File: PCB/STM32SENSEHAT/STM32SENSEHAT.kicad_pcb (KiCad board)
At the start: 2 copper layers, 100 x 100 mm, 78 parts, among them J1 USB_B_Micro, J10 Conn_01x01_Pin, J11 Conn_01x02_Pin, J2 Conn_01x05_Pin, J5 Conn_01x24_Pin, J8 Conn_01x24_Pin, J9 Conn_01x10_Pin, Q1 FS8205A, SW1 SW_Push, U1 MCP1700x-330xxTT, U11 AO3401A_C306862, U2 DW01A, U3 FT234XD-R, U4 TMP102xxDRL, U5 CAT24C256, U6 LTR-303ALS-01, U7 TP4056, U9 STLINK_UCT, X1 XXDCELNANF-8MHZ

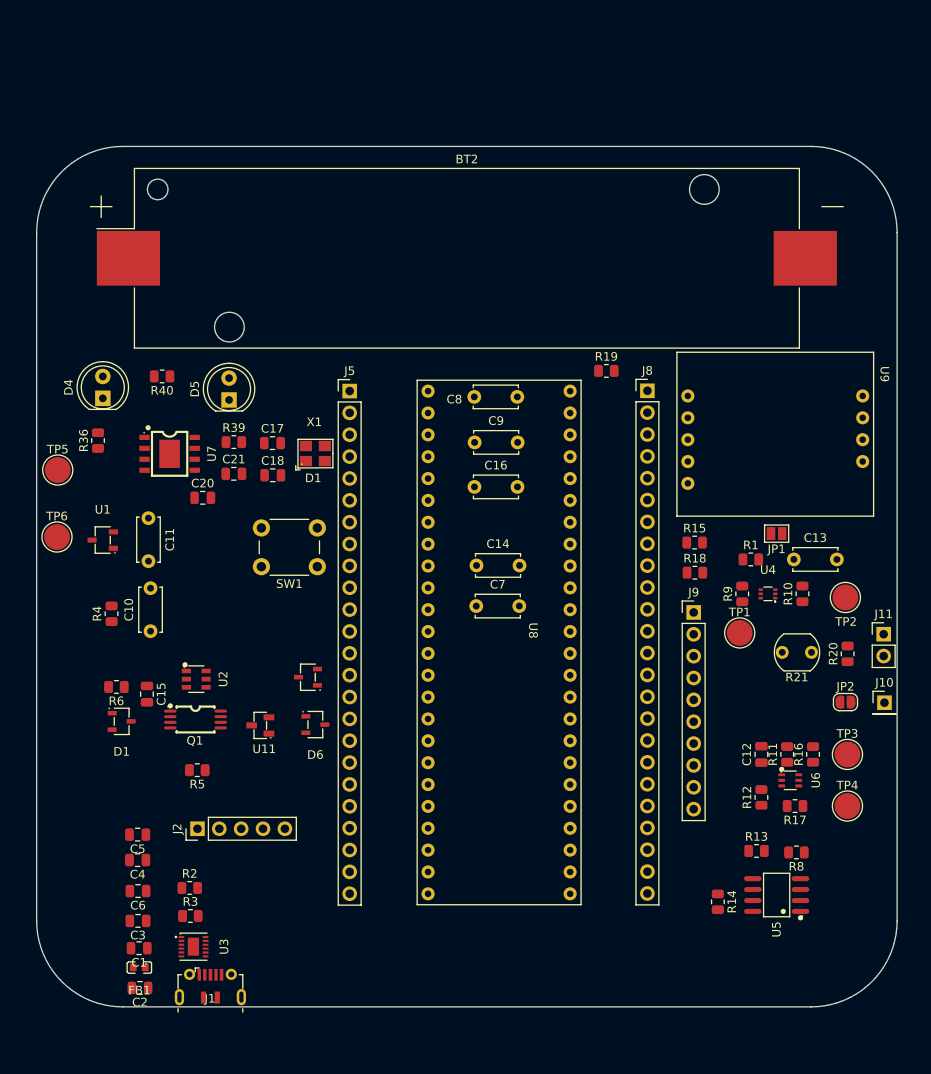
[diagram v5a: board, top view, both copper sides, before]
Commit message: New PCB with tracks laid
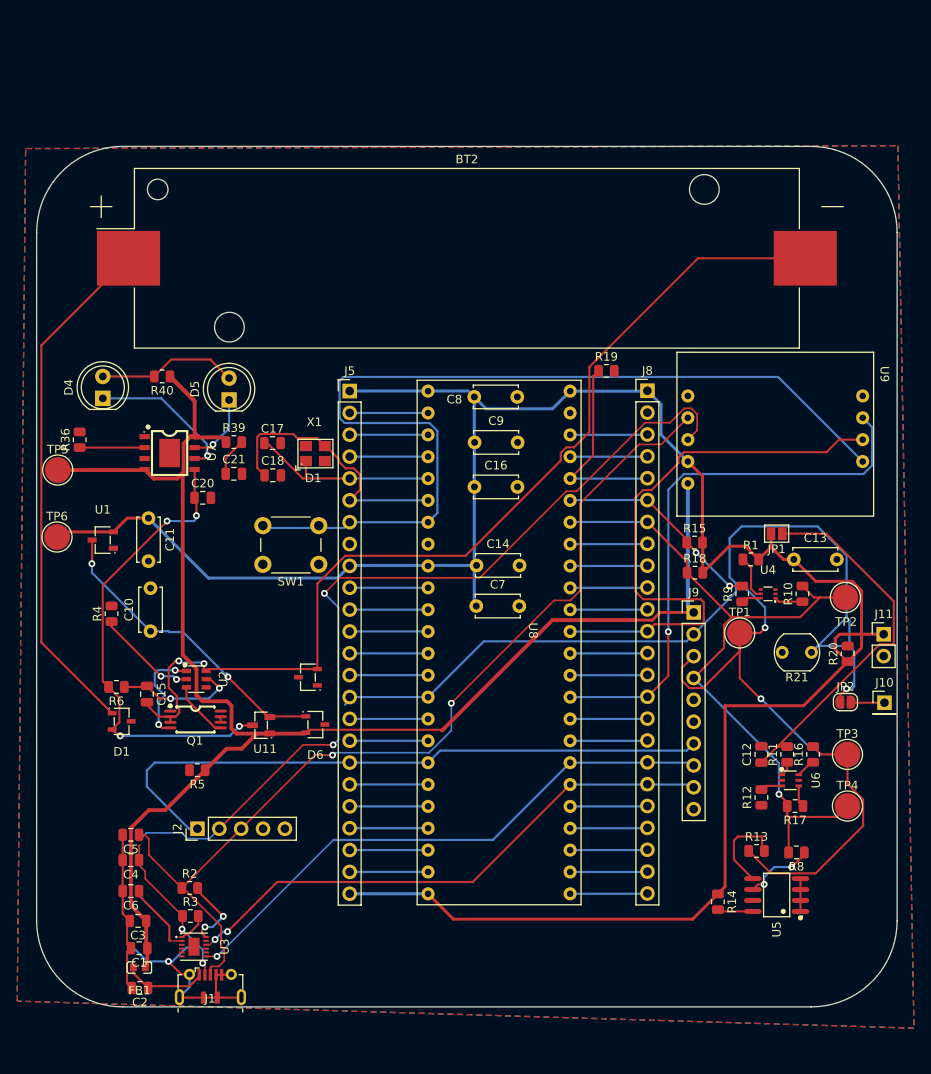
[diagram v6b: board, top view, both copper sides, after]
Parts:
- moved R36 2.13 mm to (105.0, 74.1)
- moved C6 0.83 mm to (111.0, 126.5)
- moved C5 0.79 mm to (111.0, 120.0)
- moved C4 0.79 mm to (111.0, 122.9)
- moved SW1 0.32 mm to (132.8, 88.6)
- moved U11 0.10 mm to (126.1, 107.3)
- moved U7 0.09 mm to (115.5, 75.6)
- moved U3 0.05 mm to (118.3, 133.0)
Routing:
- net 3V3: track 0.00 -> 264.2 mm
- net 5VUSB: track 0.00 -> 179.3 mm
- net /MCU MODULE/USB_DN: track 0.00 -> 120.5 mm, vias 0 -> 4
- net Net-(BT2--): track 0.00 -> 117.1 mm, vias 0 -> 2
- net /MCU MODULE/NRST: track 0.00 -> 112.1 mm
- net /MCU MODULE/USB_DP: track 0.00 -> 111.4 mm, vias 0 -> 2
- net /MCU MODULE/PA5: track 0.00 -> 102.0 mm, vias 0 -> 1
- net /MCU MODULE/PB7: track 0.00 -> 95.5 mm, vias 0 -> 4
- net /MCU MODULE/PB0: track 0.00 -> 84.4 mm
- net /MCU MODULE/PB6: track 0.00 -> 82.6 mm, vias 0 -> 1
- net /MCU MODULE/PA14: track 0.00 -> 67.3 mm
- net /MCU MODULE/PA10: track 0.00 -> 66.5 mm, vias 0 -> 1
- net /MCU MODULE/PA13: track 0.00 -> 64.9 mm, vias 0 -> 1
- net /MCU MODULE/PA9: track 0.00 -> 64.6 mm, vias 0 -> 2
- net GND: track 0.00 -> 60.5 mm, vias 0 -> 1
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- added copper zone on B.Cu, net GND
- added copper zone on F.Cu, net GND

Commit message: Slight PCB changes
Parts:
- added C19: 100nF, Capacitor_THT:C_Disc_D5.0mm_W2.5mm_P5.00mm, F.Cu at (121.4, 95.9)
- C17, C18: value 10nF -> 10pF; footprint Capacitor_SMD:C_0805_2012Metric -> Capacitor_THT:C_Disc_D5.0mm_W2.5mm_P5.00mm
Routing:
- net /MCU MODULE/PB0: track 84.4 -> 128.2 mm, vias 0 -> 1
- net GND: track 60.5 -> 54.4 mm, vias 1 -> 2
- net 5VUSB: track 179.3 -> 183.3 mm

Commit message: Updated PCB with latest changes
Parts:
- added C19: 100nF, Capacitor_THT:C_Disc_D5.0mm_W2.5mm_P5.00mm, F.Cu at (122.1, 88.8)
- added D2: LED, LED_THT:LED_D5.0mm, F.Cu at (102.6, 92.2)
- added R7: 1k0, Resistor_SMD:R_0805_2012Metric, F.Cu at (103.3, 97.9)
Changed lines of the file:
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@@
   (net 85 "unconnected-(U6-INT-Pad5)")
   (net 86 "Net-(BT2-+)")
+  (net 87 "Net-(D2-A)")
   (footprint "JLCfootprint:SOT-23-3_L3.0-W1.7-P0.95-LS2.9-BR" (layer "F.Cu")
     (at 109.874987 106.82 180)
@@
   )
   (footprint "Resistor_SMD:R_0805_2012Metric" (layer "F.Cu")
+    (at 103.2975 97.91)
+    (descr "Resistor SMD 0805 (2012 Metric), square (rectangular) end terminal, IPC_7351 nominal, (Body size source: IPC-SM-782 page 72, https://www.pcb-3d.com/wordpress/wp-content/uploads/ipc-sm-782a_amendment_1_and_2.pdf), generated with kicad-footprint-generator")
+    (tags "resistor")
+    (property "Basic" "")
+    (property "DNP" "")
+    (property "Extended" "")
+    (property "MOQ and Attrition" "")
+    (property "Price" "")
+    (property "Sheetfile" "power.kicad_sch")
+    (property "Sheetname" "POWER MANAGEMENT MODULE")
+    (property "ki_description" "Resistor, small symbol")
+    (property "ki_keywords" "R resistor")
+    (attr smd)
+    (fp_text reference "R7" (at 0 -1.65) (layer "F.SilkS")
+        (effects (font (size 1 1) (thickness 0.15)))
+    )
+    (fp_text value "1k0" (at 0 1.65) (layer "F.Fab")
+        (effects (font (size 1 1) (thickness 0.15)))
+    )
+    (fp_text user "${REFERENCE}" (at 0 0) (layer "F.Fab")
+        (effects (font (size 0.5 0.5) (thickness 0.08)))
+    )
+    (fp_line (start -0.227064 -0.735) (end 0.227064 -0.735)
+      (stroke (width 0.12) (type solid)) (layer "F.SilkS"))
+    (fp_line (start -0.227064 0.735) (end 0.227064 0.735)
+      (stroke (width 0.12) (type solid)) (layer "F.SilkS"))
+    (fp_line (start -1.68 -0.95) (end 1.68 -0.95)
+      (stroke (width 0.05) (type solid)) (layer "F.CrtYd"))
+    (fp_line (start -1.68 0.95) (end -1.68 -0.95)
+      (stroke (width 0.05) (type solid)) (layer "F.CrtYd"))
+    (fp_line (start 1.68 -0.95) (end 1.68 0.95)
+      (stroke (width 0.05) (type solid)) (layer "F.CrtYd"))
+    (fp_line (start 1.68 0.95) (end -1.68 0.95)
+      (stroke (width 0.05) (type solid)) (layer "F.CrtYd"))
+    (fp_line (start -1 -0.625) (end 1 -0.625)
+      (stroke (width 0.1) (type solid)) (layer "F.Fab"))
+    (fp_line (start -1 0.625) (end -1 -0.625)
+      (stroke (width 0.1) (type solid)) (layer "F.Fab"))
+    (fp_line (start 1 -0.625) (end 1 0.625)
+      (stroke (width 0.1) (type solid)) (layer "F.Fab"))
+    (fp_line (start 1 0.625) (end -1 0.625)
+      (stroke (width 0.1) (type solid)) (layer "F.Fab"))
+    (pad "1" smd roundrect (at -0.9125 0) (size 1.025 1.4) (layers "F.Cu" "F.Paste" "F.Mask") (roundrect_rratio 0.243902)
+      (net 11 "3V3") (pintype "passive"))
+    (pad "2" smd roundrect (at 0.9125 0) (size 1.025 1.4) (layers "F.Cu" "F.Paste" "F.Mask") (roundrect_rratio 0.243902)
+      (net 87 "Net-(D2-A)") (pintype "passive"))
+    (model "${KICAD6_3DMODEL_DIR}/Resistor_SMD.3dshapes/R_0805_2012Metric.wrl"
+      (offset (xyz 0 0 0))
+      (scale (xyz 1 1 1))
+      (rotate (xyz 0 0 0))
+    )
+  )
+  (footprint "Resistor_SMD:R_0805_2012Metric" (layer "F.Cu")
     (at 189 92 90)
     (descr "Resistor SMD 0805 (2012 Metric), square (rectangular) end terminal, IPC_7351 nominal, (Body size source: IPC-SM-782 page 72, https://www.pcb-3d.com/wordpress/wp-content/uploads/ipc-sm-782a_amendment_1_and_2.pdf), generated with kicad-footprint-generator")
@@
     )
   )
+  (footprint "LED_THT:LED_D5.0mm" (layer "F.Cu")
+    (at 102.645 92.24)
+    (descr "LED, diameter 5.0mm, 2 pins, http://cdn-reichelt.de/documents/datenblatt/A500/LL-504BC2E-009.pdf")
+    (tags "LED diameter 5.0mm 2 pins")
+    (property "Basic" "")
+    (property "DNP" "")
+    (property "Extended" "")
+    (property "MOQ and Attrition" "")
+    (property "Price" "")
+    (property "Sheetfile" "power.kicad_sch")
+    (property "Sheetname" "POWER MANAGEMENT MODULE")
+    (property "ki_description" "Light emitting diode")
+    (property "ki_keywords" "LED diode")
+    (attr through_hole)
+    (fp_text reference "D2" (at 1.27 -3.96) (layer "F.SilkS")
+        (effects (font (size 1 1) (thickness 0.15)))
+    )
+    (fp_text value "LED" (at 1.27 3.96) (layer "F.Fab")
+        (effects (font (size 1 1) (thickness 0.15)))
+    )
+    (fp_text user "${REFERENCE}" (at 1.25 0) (layer "F.Fab")
+        (effects (font (size 0.8 0.8) (thickness 0.2)))
+    )
+    (fp_line (start -1.29 -1.545) (end -1.29 1.545)
+      (stroke (width 0.12) (type solid)) (layer "F.SilkS"))
+    (fp_arc (start -1.29 -1.54483) (mid 2.072002 -2.880433) (end 4.26 0.000462)
+      (stroke (width 0.12) (type solid)) (layer "F.SilkS"))
+    (fp_arc (start 4.26 -0.000462) (mid 2.072002 2.880433) (end -1.29 1.54483)
+      (stroke (width 0.12) (type solid)) (layer "F.SilkS"))
+    (fp_circle (center 1.27 0) (end 3.77 0)
+      (stroke (width 0.12) (type solid)) (fill none) (layer "F.SilkS"))
+    (fp_line (start -1.95 -3.25) (end -1.95 3.25)
+      (stroke (width 0.05) (type solid)) (layer "F.CrtYd"))
+    (fp_line (start -1.95 3.25) (end 4.5 3.25)
+      (stroke (width 0.05) (type solid)) (layer "F.CrtYd"))
+    (fp_line (start 4.5 -3.25) (end -1.95 -3.25)
+      (stroke (width 0.05) (type solid)) (layer "F.CrtYd"))
+    (fp_line (start 4.5 3.25) (end 4.5 -3.25)
+      (stroke (width 0.05) (type solid)) (layer "F.CrtYd"))
+    (fp_line (start -1.23 -1.469694) (end -1.23 1.469694)
+      (stroke (width 0.1) (type solid)) (layer "F.Fab"))
+    (fp_arc (start -1.23 -1.469694) (mid 4.17 0.000016) (end -1.230016 1.469666)
+      (stroke (width 0.1) (type solid)) (layer "F.Fab"))
+    (fp_circle (center 1.27 0) (end 3.77 0)
+      (stroke (width 0.1) (type solid)) (fill none) (layer "F.Fab"))
+    (pad "1" thru_hole rect (at 0 0) (size 1.8 1.8) (drill 0.9) (layers "*.Cu" "*.Mask")
+      (net 2 "GND") (pinfunction "K") (pintype "passive"))
+    (pad "2" thru_hole circle (at 2.54 0) (size 1.8 1.8) (drill 0.9) (layers "*.Cu" "*.Mask")
+      (net 87 "Net-(D2-A)") (pinfunction "A") (pintype "passive"))
+    (model "${KICAD6_3DMODEL_DIR}/LED_THT.3dshapes/LED_D5.0mm.wrl"
+      (offset (xyz 0 0 0))
+      (scale (xyz 1 1 1))
+      (rotate (xyz 0 0 0))
+    )
+  )
   (footprint "Connector_PinHeader_2.54mm:PinHeader_1x24_P2.54mm_Vertical" (layer "F.Cu")
     (at 136.38 68.43)
@@
     )
   )
+  (footprint "Capacitor_THT:C_Disc_D5.0mm_W2.5mm_P5.00mm" (layer "F.Cu")
+    (at 122.09 88.77 90)
+    (descr "C, Disc series, Radial, pin pitch=5.00mm, , diameter*width=5*2.5mm^2, Capacitor, http://cdn-reichelt.de/documents/datenblatt/B300/DS_KERKO_TC.pdf")
+    (tags "C Disc series Radial pin pitch 5.00mm  diameter 5mm width 2.5mm Capacitor")
+    (property "Basic" "")
+    (property "DNP" "")
+    (property "Extended" "")
+    (property "MOQ and Attrition" "")
+    (property "Price" "")
+    (property "Sheetfile" "mcu.kicad_sch")
+    (property "Sheetname" "MCU MODULE")
+    (property "ki_description" "Unpolarized capacitor, small symbol")
+    (property "ki_keywords" "capacitor cap")
+    (attr through_hole)
+    (fp_text reference "C19" (at 2.5 -2.5 90) (layer "F.SilkS")
+        (effects (font (size 1 1) (thickness 0.15)))
+    )
+    (fp_text value "100nF" (at 2.5 2.5 90) (layer "F.Fab")
+        (effects (font (size 1 1) (thickness 0.15)))
+    )
+    (fp_text user "${REFERENCE}" (at 2.5 0 90) (layer "F.Fab")
+        (effects (font (size 1 1) (thickness 0.15)))
+    )
+    (fp_line (start -0.12 -1.37) (end -0.12 -1.055)
+      (stroke (width 0.12) (type solid)) (layer "F.SilkS"))
+    (fp_line (start -0.12 -1.37) (end 5.12 -1.37)
+      (stroke (width 0.12) (type solid)) (layer "F.SilkS"))
+    (fp_line (start -0.12 1.055) (end -0.12 1.37)
+      (stroke (width 0.12) (type solid)) (layer "F.SilkS"))
+    (fp_line (start -0.12 1.37) (end 5.12 1.37)
+      (stroke (width 0.12) (type solid)) (layer "F.SilkS"))
+    (fp_line (start 5.12 -1.37) (end 5.12 -1.055)
+      (stroke (width 0.12) (type solid)) (layer "F.SilkS"))
+    (fp_line (start 5.12 1.055) (end 5.12 1.37)
+      (stroke (width 0.12) (type solid)) (layer "F.SilkS"))
+    (fp_line (start -1.05 -1.5) (end -1.05 1.5)
+      (stroke (width 0.05) (type solid)) (layer "F.CrtYd"))
+    (fp_line (start -1.05 1.5) (end 6.05 1.5)
+      (stroke (width 0.05) (type solid)) (layer "F.CrtYd"))
+    (fp_line (start 6.05 -1.5) (end -1.05 -1.5)
+      (stroke (width 0.05) (type solid)) (layer "F.CrtYd"))
+    (fp_line (start 6.05 1.5) (end 6.05 -1.5)
+      (stroke (width 0.05) (type solid)) (layer "F.CrtYd"))
+    (fp_line (start 0 -1.25) (end 0 1.25)
+      (stroke (width 0.1) (type solid)) (layer "F.Fab"))
+    (fp_line (start 0 1.25) (end 5 1.25)
+      (stroke (width 0.1) (type solid)) (layer "F.Fab"))
+    (fp_line (start 5 -1.25) (end 0 -1.25)
+      (stroke (width 0.1) (type solid)) (layer "F.Fab"))
+    (fp_line (start 5 1.25) (end 5 -1.25)
+      (stroke (width 0.1) (type solid)) (layer "F.Fab"))
+    (pad "1" thru_hole circle (at 0 0 90) (size 1.6 1.6) (drill 0.8) (layers "*.Cu" "*.Mask")
+      (net 27 "/MCU MODULE/NRST") (pintype "passive"))
+    (pad "2" thru_hole circle (at 5 0 90) (size 1.6 1.6) (drill 0.8) (layers "*.Cu" "*.Mask")
+      (net 2 "GND") (pintype "passive"))
+    (model "${KICAD6_3DMODEL_DIR}/Capacitor_THT.3dshapes/C_Disc_D5.0mm_W2.5mm_P5.00mm.wrl"
+      (offset (xyz 0 0 0))
+      (scale (xyz 1 1 1))
+      (rotate (xyz 0 0 0))
+    )
+  )
